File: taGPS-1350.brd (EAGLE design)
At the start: 49.9 x 61.5 mm, 84 parts, among them IC1 MSP430FR698X(1)80-PIN_PN, IC3 FT232RL

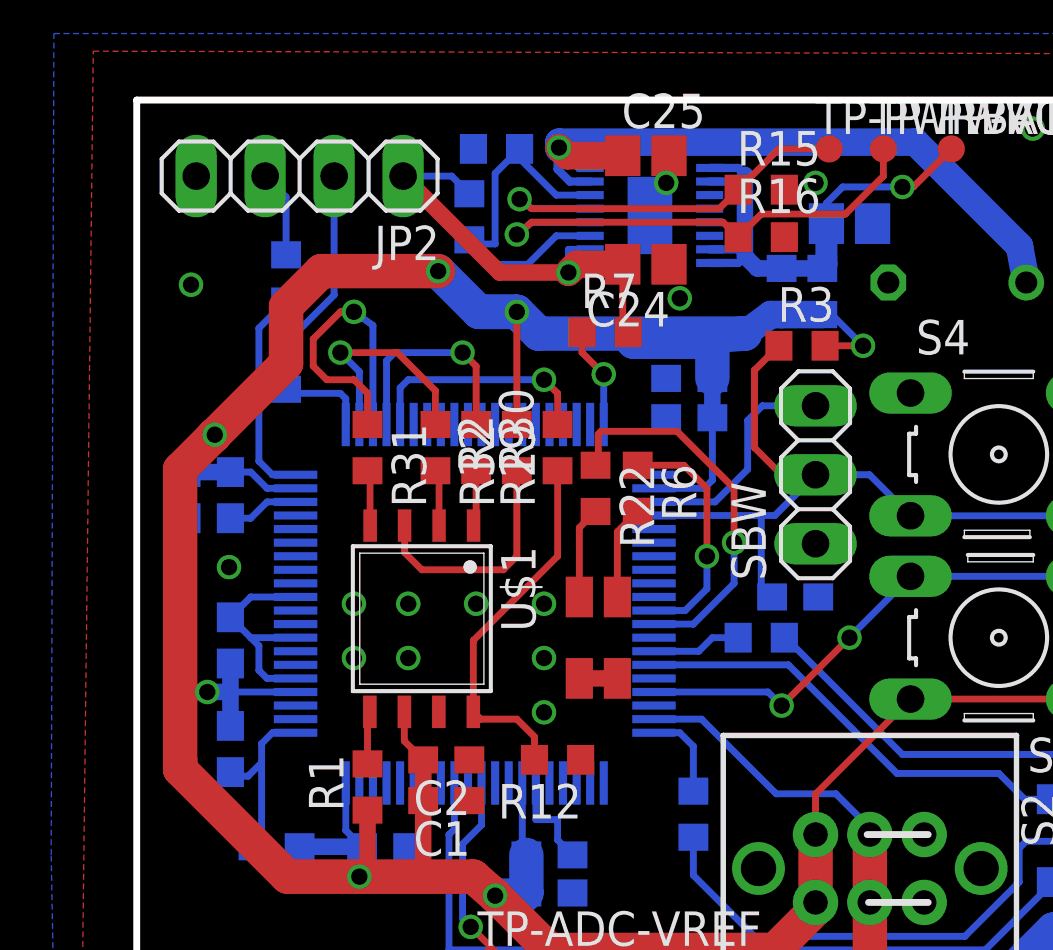
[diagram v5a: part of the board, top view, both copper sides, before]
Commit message: Remove DC power shunts
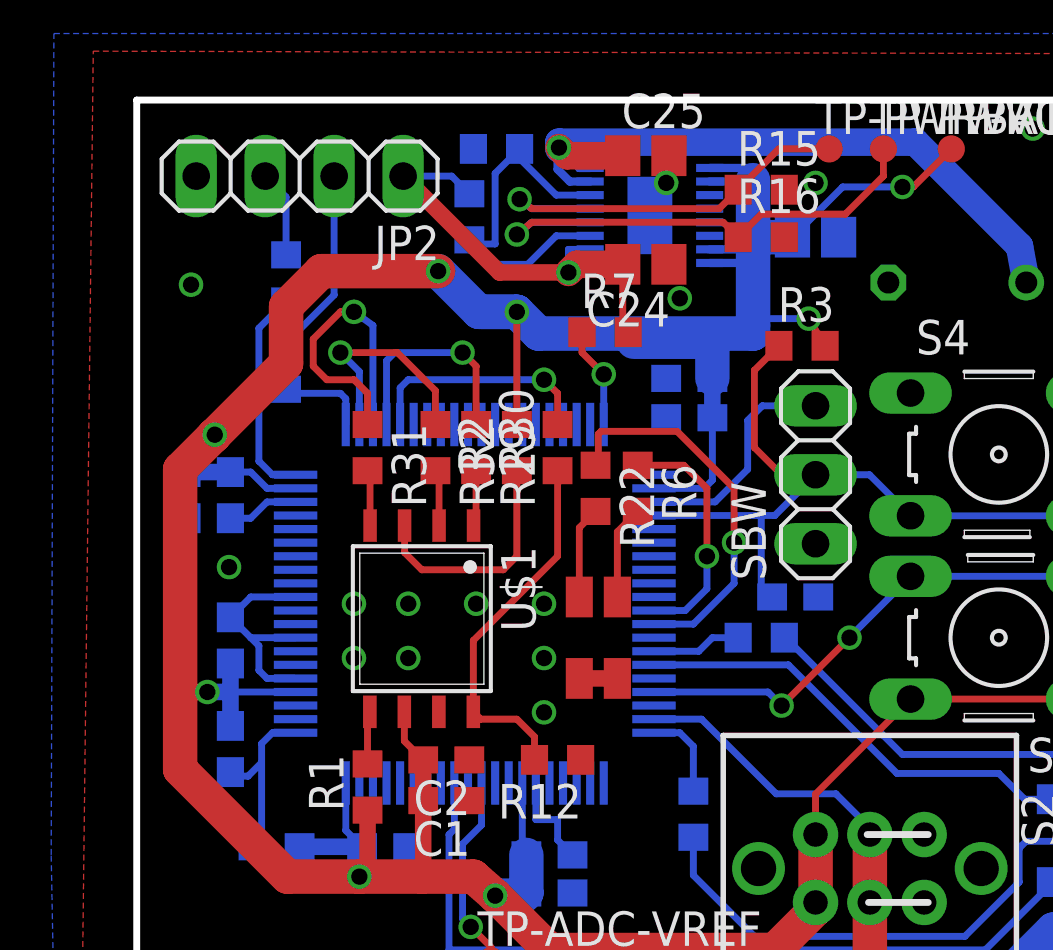
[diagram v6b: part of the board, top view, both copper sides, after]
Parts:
- removed R18, R25: 0, tagps:R0603
- moved C18 1.35 mm to (25.0, 56.5)
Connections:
- removed net N$26: C18.1, R18.1, R25.1, TP-VCC.TP, U$2.10, U$2.15, U$2.16, U$2.9
- net VCC: now also C18.1, TP-VCC.TP, U$2.10, U$2.15, U$2.16, U$2.9; no longer R18.2, R25.2
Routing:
- net N$26: track 19.5 -> 0.00 mm, vias 1 -> 0
- net VCC: track 139.4 -> 156.3 mm, vias 7 -> 8
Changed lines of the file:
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@@
 <setting verticaltext="up"/>
 </settings>
-<grid distance="0.5" unitdist="mm" unit="mm" style="lines" multiple="1" display="yes" altdistance="0.025" altunitdist="inch" altunit="inch"/>
+<grid distance="0.25" unitdist="mm" unit="mm" style="lines" multiple="1" display="yes" altdistance="0.025" altunitdist="inch" altunit="inch"/>
 <layers>
 <layer number="1" name="Top" color="4" fill="1" visible="yes" active="yes"/>
@@
 <attribute name="SPICEPREFIX" value="C" x="24.25" y="43.25" size="1.778" layer="28" rot="MR180" display="off"/>
 </element>
-<element name="C18" library="tagps" package="C0805" value="4.7uF at least" x="26.25" y="57" rot="MR180">
-<attribute name="SPICEPREFIX" value="C" x="26.25" y="57" size="1.778" layer="28" rot="MR180" display="off"/>
+<element name="C18" library="tagps" package="C0805" value="4.7uF at least" x="25" y="56.5" rot="MR180">
+<attribute name="SPICEPREFIX" value="C" x="25" y="56.5" size="1.778" layer="28" rot="MR180" display="off"/>
 </element>
 <element name="C19" library="tagps" package="C0603" value="100nF" x="22.1" y="21.6">
@@
 <attribute name="SPICEPREFIX" value="R" x="40.6" y="51.95" size="1.778" layer="28" rot="MR270" display="off"/>
 </element>
-<element name="R18" library="tagps" package="R0603" value="0" x="25.25" y="54.5" rot="MR270">
-<attribute name="SPICEPREFIX" value="R" x="25.25" y="54.5" size="1.778" layer="28" rot="MR270" display="off"/>
-</element>
 <element name="JP1" library="tagps" package="1X04" value="" x="23.9" y="1.7"/>
 <element name="JP2" library="tagps" package="1X04" value="" x="6" y="58.75" rot="R180"/>
@@
 <element name="R20" library="tagps" package="R0603" value="100" x="25.1" y="5.3" rot="R270">
 <attribute name="SPICEPREFIX" value="R" x="25.1" y="5.3" size="1.778" layer="27" rot="R270" display="off"/>
-</element>
-<element name="R25" library="tagps" package="R0603" value="0" x="23.75" y="54.5" rot="MR270">
-<attribute name="SPICEPREFIX" value="R" x="23.75" y="54.5" size="1.778" layer="28" rot="MR270" display="off"/>
 </element>
 <element name="R26" library="tagps" package="R0603" value="0" x="17.3" y="22.9" rot="R90">
@@
 <contactref element="S2" pad="3.2"/>
 <contactref element="S2" pad="3.1"/>
-<contactref element="R25" pad="2"/>
-<contactref element="R18" pad="2"/>
 <wire x1="2.775" y1="49.125" x2="2.875" y2="49.225" width="1.27" layer="1"/>
 <wire x1="2.875" y1="49.225" x2="1.6" y2="47.95" width="1.27" layer="1"/>
 <wire x1="1.6" y1="47.95" x2="1.6" y2="39.55" width="1.27" layer="1"/>
-<wire x1="1.6" y1="39.55" x2="1.6" y2="37.25" width="1.27" layer="1"/>
-<wire x1="1.6" y1="37.25" x2="1.6" y2="37" width="1.27" layer="1"/>
+<wire x1="1.6" y1="39.55" x2="1.6" y2="36.9" width="1.27" layer="1"/>
 <wire x1="12.7" y1="53.75" x2="14" y2="53.75" width="1.27" layer="16"/>
 <via x="11.1" y="55.25" extent="1-16" drill="0.6"/>
@@
 <wire x1="8.5" y1="33.25" x2="8.5" y2="35.4" width="0.6096" layer="1"/>
 <wire x1="14" y1="53.75" x2="14.8" y2="52.95" width="1.27" layer="16"/>
-<wire x1="14.8" y1="52.95" x2="22.4" y2="52.95" width="1.27" layer="16"/>
-<wire x1="22.4" y1="52.95" x2="18.3" y2="52.65" width="1.27" layer="16"/>
+<wire x1="14.8" y1="52.95" x2="22.7" y2="52.95" width="1.27" layer="16"/>
 <wire x1="18.3" y1="52.65" x2="21.2" y2="52.65" width="1.27" layer="16"/>
 <wire x1="21.2" y1="52.65" x2="21.2" y2="51.3" width="1.27" layer="16"/>
 <wire x1="11.1" y1="55.25" x2="12.6" y2="53.75" width="1.27" layer="16"/>
 <wire x1="12.6" y1="53.75" x2="14" y2="53.75" width="1.27" layer="16"/>
-<wire x1="22.4" y1="52.95" x2="23.35" y2="53.65" width="1.016" layer="16"/>
-<wire x1="23.35" y1="53.65" x2="23.75" y2="53.65" width="1.016" layer="16"/>
-<wire x1="23.75" y1="53.65" x2="25.25" y2="53.65" width="1.016" layer="16"/>
 <wire x1="25" y1="34.5" x2="25" y2="35.9906" width="0.254" layer="1"/>
 <wire x1="25" y1="35.9906" x2="28.4988" y2="39.4894" width="0.254" layer="1"/>
@@
 <wire x1="5.5" y1="51.85" x2="5.5" y2="53.95" width="1.27" layer="1"/>
 <wire x1="5.5" y1="53.95" x2="6.8" y2="55.25" width="1.27" layer="1"/>
-<wire x1="25.35" y1="52.5" x2="26.75" y2="52.5" width="0.254" layer="1"/>
-<via x="26.75" y="52.5" extent="1-16" drill="0.6"/>
-<wire x1="26.75" y1="52.5" x2="25.6" y2="53.65" width="0.254" layer="16"/>
-<wire x1="25.6" y1="53.65" x2="25.25" y2="53.65" width="0.254" layer="16"/>
+<wire x1="25.35" y1="52.5" x2="24.75" y2="53.5" width="0.254" layer="1"/>
+<via x="24.75" y="53.5" extent="1-16" drill="0.6"/>
 <wire x1="5.55" y1="32.95" x2="1.6" y2="36.9" width="1.27" layer="1"/>
-<wire x1="1.6" y1="36.9" x2="1.6" y2="37" width="1.27" layer="1"/>
+<contactref element="U$2" pad="9"/>
+<contactref element="U$2" pad="10"/>
+<contactref element="U$2" pad="15"/>
+<contactref element="U$2" pad="16"/>
+<contactref element="C18" pad="1"/>
+<contactref element="TP-VCC" pad="TP"/>
+<wire x1="21.1" y1="59.05" x2="22.7" y2="59.05" width="0.3048" layer="16"/>
+<wire x1="21.1" y1="58.55" x2="22.15" y2="58.55" width="0.3048" layer="16"/>
+<wire x1="22.15" y1="58.55" x2="22.4" y2="58.8" width="0.3048" layer="16"/>
+<wire x1="21.1" y1="56.05" x2="22.15" y2="56.05" width="0.3048" layer="16"/>
+<wire x1="22.15" y1="56.05" x2="22.4" y2="55.8" width="0.3048" layer="16"/>
+<wire x1="22.4" y1="55.8" x2="22.15" y2="55.55" width="0.3048" layer="16"/>
+<wire x1="22.15" y1="55.55" x2="21.1" y2="55.55" width="0.3048" layer="16"/>
+<via x="28.2" y="58.35" extent="1-16" drill="0.6"/>
+<wire x1="28.2" y1="58.35" x2="28.6" y2="58.35" width="0.254" layer="1"/>
+<wire x1="28.6" y1="58.35" x2="30" y2="59.75" width="0.254" layer="1"/>
+<wire x1="28.2" y1="58.35" x2="26" y2="58.35" width="0.254" layer="16"/>
+<wire x1="26" y1="58.35" x2="24.15" y2="56.5" width="0.254" layer="16"/>
+<wire x1="22.7" y1="52.95" x2="22.7" y2="53.25" width="1.27" layer="16"/>
+<wire x1="22.7" y1="53.25" x2="22.7" y2="53.5" width="1.27" layer="16"/>
+<wire x1="22.7" y1="53.5" x2="22.7" y2="56.25" width="1.27" layer="16"/>
+<wire x1="22.7" y1="56.25" x2="22.7" y2="56.5" width="1.27" layer="16"/>
+<wire x1="22.7" y1="56.5" x2="22.7" y2="58.6" width="1.27" layer="16"/>
+<wire x1="22.7" y1="59.05" x2="22.7" y2="58.6" width="0.3048" layer="16"/>
+<wire x1="24.15" y1="56.5" x2="22.7" y2="56.5" width="1.27" layer="16"/>
+<wire x1="24.75" y1="53.5" x2="22.7" y2="53.5" width="0.254" layer="16"/>
+<wire x1="21.2" y1="52.65" x2="22.7" y2="52.65" width="0.254" layer="16"/>
+<wire x1="22.7" y1="52.65" x2="22.7" y2="53.25" width="0.254" layer="16"/>
+<wire x1="22.15" y1="56.05" x2="22.7" y2="56.05" width="0.254" layer="16"/>
+<wire x1="22.7" y1="56.05" x2="22.7" y2="56.25" width="0.254" layer="16"/>
+<wire x1="22.7" y1="58.6" x2="22.4" y2="58.6" width="0.254" layer="16"/>
+<wire x1="22.4" y1="58.6" x2="22.4" y2="58.8" width="0.254" layer="16"/>
 </signal>
 <signal name="GND">
@@
 <wire x1="27.5" y1="58.75" x2="27.5" y2="59.75" width="0.254" layer="1"/>
 </signal>
-<signal name="N$26">
-<contactref element="U$2" pad="9"/>
-<contactref element="U$2" pad="10"/>
-<contactref element="U$2" pad="15"/>
-<contactref element="U$2" pad="16"/>
-<contactref element="C18" pad="1"/>
-<contactref element="TP-VCC" pad="TP"/>
-<wire x1="21.1" y1="59.05" x2="22.15" y2="59.05" width="0.3048" layer="16"/>
-<wire x1="22.15" y1="59.05" x2="22.4" y2="58.8" width="0.3048" layer="16"/>
-<wire x1="21.1" y1="58.55" x2="22.15" y2="58.55" width="0.3048" layer="16"/>
-<wire x1="22.15" y1="58.55" x2="22.4" y2="58.8" width="0.3048" layer="16"/>
-<wire x1="21.1" y1="56.05" x2="22.15" y2="56.05" width="0.3048" layer="16"/>
-<wire x1="22.15" y1="56.05" x2="22.4" y2="55.8" width="0.3048" layer="16"/>
-<wire x1="22.4" y1="55.8" x2="22.15" y2="55.55" width="0.3048" layer="16"/>
-<wire x1="22.15" y1="55.55" x2="21.1" y2="55.55" width="0.3048" layer="16"/>
-<contactref element="R25" pad="1"/>
-<contactref element="R18" pad="1"/>
-<wire x1="22.4" y1="55.8" x2="22.4" y2="58.8" width="0.6096" layer="16"/>
-<wire x1="25.25" y1="55.35" x2="23.75" y2="55.35" width="0.6096" layer="16"/>
-<wire x1="22.4" y1="55.8" x2="22.85" y2="55.35" width="0.6096" layer="16"/>
-<wire x1="22.85" y1="55.35" x2="23.75" y2="55.35" width="0.6096" layer="16"/>
-<via x="28.2" y="58.35" extent="1-16" drill="0.6"/>
-<wire x1="25.4" y1="57" x2="25.4" y2="55.5" width="0.8128" layer="16"/>
-<wire x1="25.4" y1="55.5" x2="25.25" y2="55.35" width="0.8128" layer="16"/>
-<wire x1="28.2" y1="58.35" x2="28.6" y2="58.35" width="0.254" layer="1"/>
-<wire x1="28.6" y1="58.35" x2="30" y2="59.75" width="0.254" layer="1"/>
-<wire x1="28.2" y1="58.35" x2="26" y2="58.35" width="0.254" layer="16"/>
-<wire x1="26" y1="58.35" x2="25.4" y2="57.75" width="0.254" layer="16"/>
-<wire x1="25.4" y1="57.75" x2="25.4" y2="57" width="0.254" layer="16"/>
-</signal>
 <signal name="N$32">

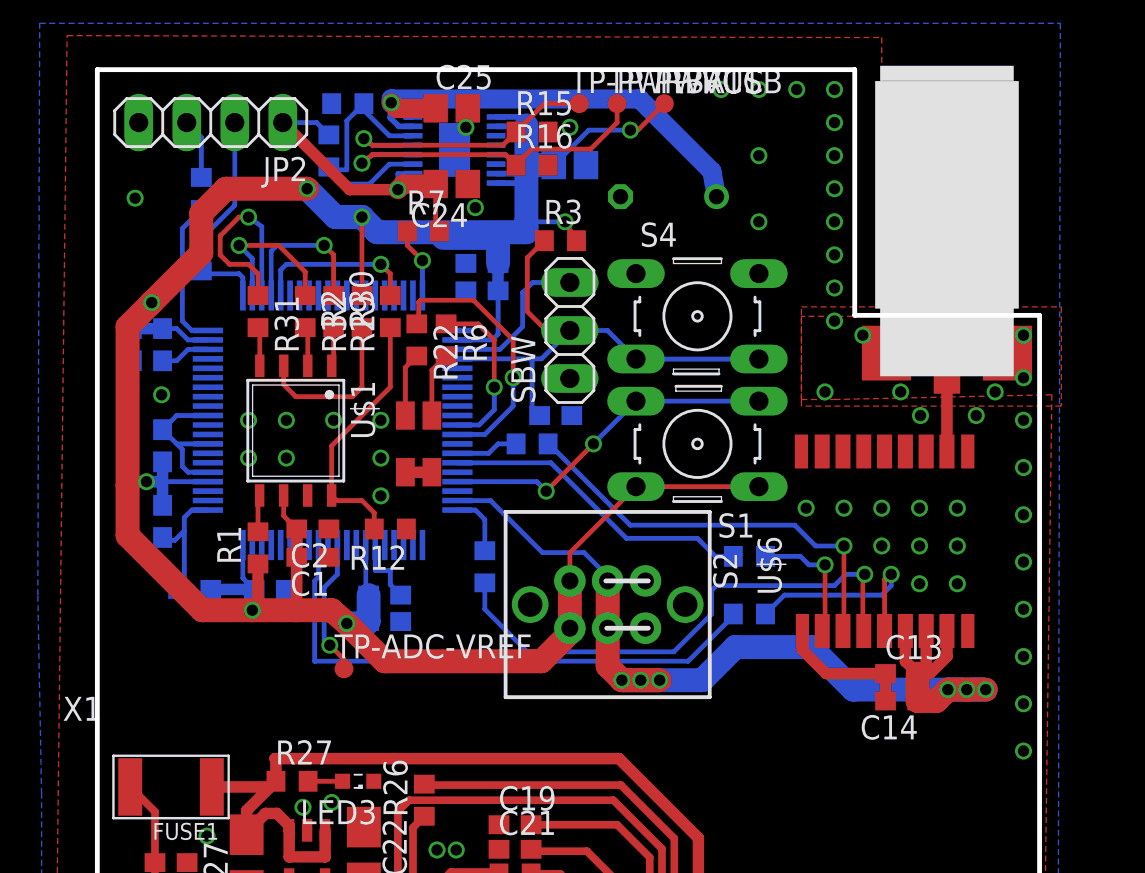
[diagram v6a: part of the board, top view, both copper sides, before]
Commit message: Add Ferrite Beads for GPS chip, modify battery input
For battery input one capacitor package was modified...
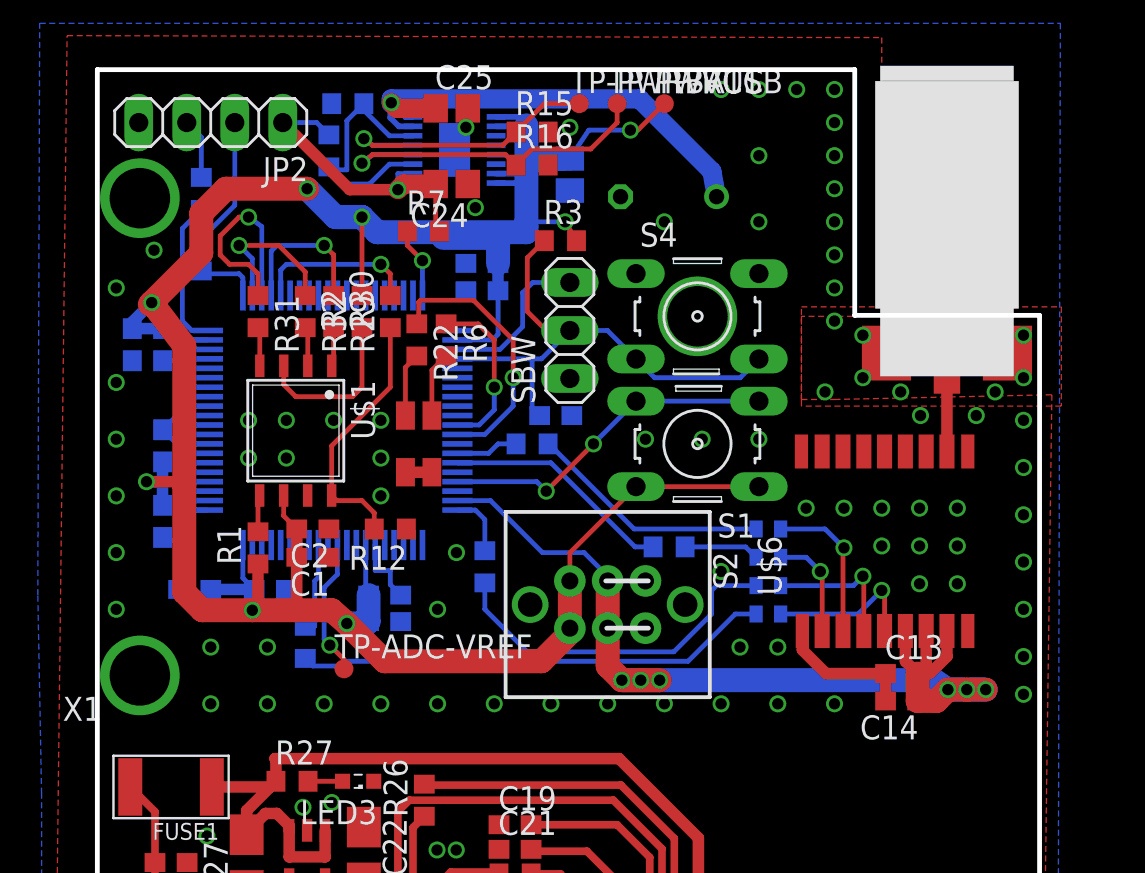
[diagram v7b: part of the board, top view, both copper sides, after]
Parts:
- added FB0, FB1, FB2, FB3: (no value), tagps:R0402
- moved R34 23.5 mm to (11.0, 31.2), turned to 270 degrees
- moved R28 4.28 mm to (30.2, 36.3)
- moved C18 0.50 mm to (25.0, 56.0), turned to 270 degrees
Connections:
- new net N$15: FB0.2, U$6.3
- new net N$26: FB1.2, U$6.2
- new net N$49: FB2.1, U$6.4
- new net N$50: FB3.1, U$6.5
- net MB-GPS-RX: now also FB0.1; no longer U$6.3
- net MB-GPS-TX: now also FB1.1; no longer U$6.2
- net N$46: now also FB3.2; no longer U$6.5
- net N$47: now also FB2.2; no longer U$6.4
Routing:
- net MB-GPS-WAKEUP: track 29.5 -> 4.88 mm
- net N$46: track 11.1 -> 25.2 mm, vias 1 -> 0
- net MB-GPS-RX: track 22.4 -> 12.9 mm, vias 1 -> 0
- net N$47: track 27.9 -> 18.9 mm, vias 1 -> 0
- net N$15: track 0.00 -> 8.18 mm, vias 0 -> 1
- net N$50: track 0.00 -> 8.08 mm, vias 0 -> 1
- net N$49: track 0.00 -> 7.48 mm, vias 0 -> 1
- net N$26: track 0.00 -> 5.60 mm, vias 0 -> 1
- net N$45: track 16.7 -> 12.2 mm
- net MB-GPS-TX: track 6.90 -> 3.98 mm, vias 1 -> 0
- net MB-PWR_GPS_SENSE: track 51.9 -> 50.3 mm
- net SBW-TDO/TDI: track 27.2 -> 28.0 mm
- net GND: vias 71 -> 99
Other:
- board text added: "taGPS v1350-0.31"
- board text removed: "taGPS v1350-0.3"
